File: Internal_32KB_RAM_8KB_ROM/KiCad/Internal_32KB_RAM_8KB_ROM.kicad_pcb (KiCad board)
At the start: 2 copper layers, 82.9 x 61 mm, 14 parts, among them J1 UD4, J2 UE4, J3 RAM Decoder, J4 BLK Decoder, J5 Disable/Enable Switch, U1 ATF16V8, U2 74HCT138, U3 62256, U4 2864

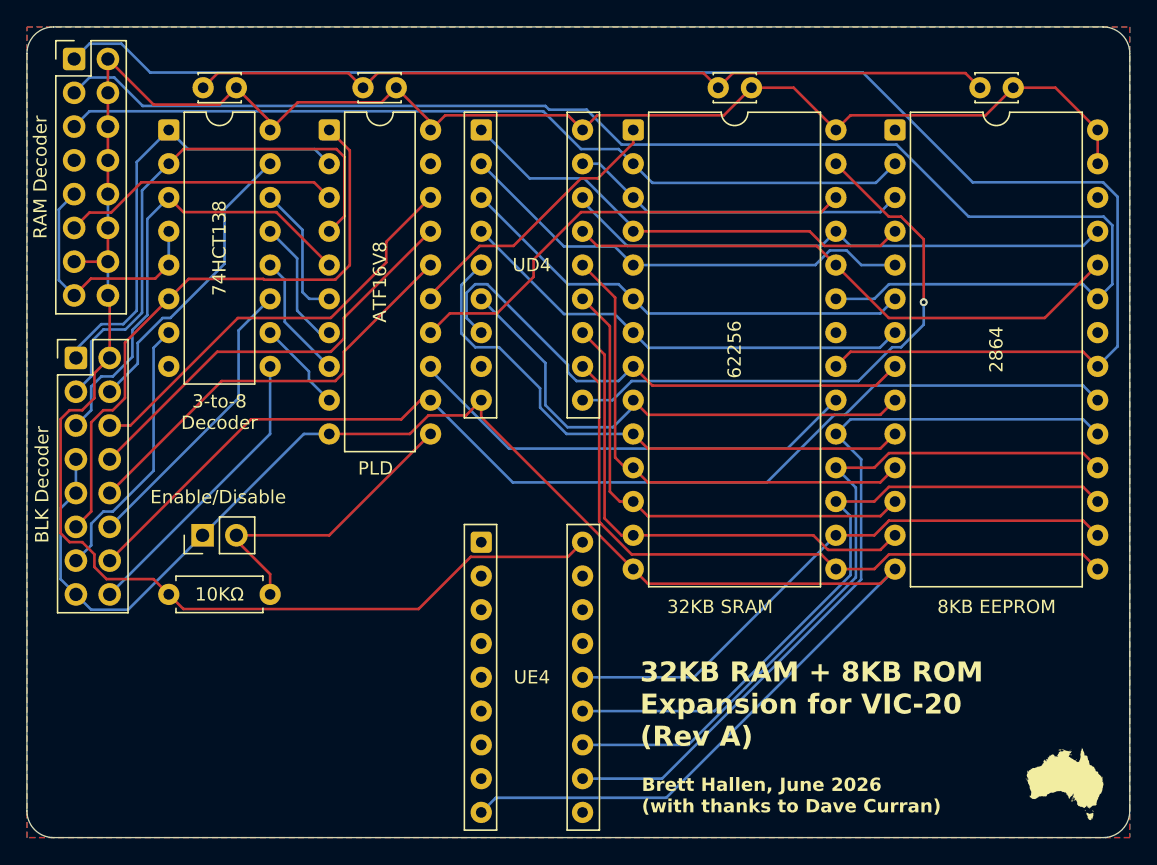
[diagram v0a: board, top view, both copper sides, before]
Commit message: Finalised 40KB design for testing
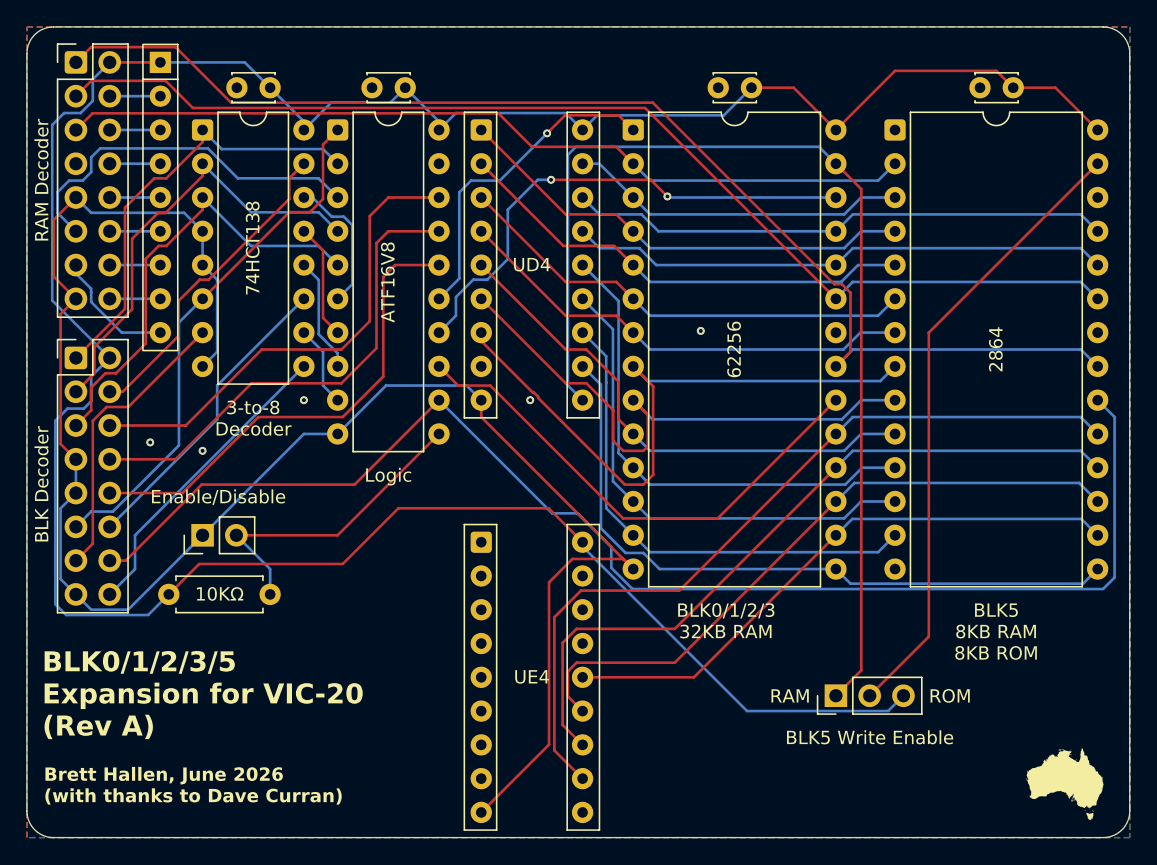
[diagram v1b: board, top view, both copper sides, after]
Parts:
- added J6: BLK5 Write Enable, Connector_PinHeader_2.54mm:PinHeader_1x03_P2.54mm_Vertical, F.Cu at (126.8, 83.2)
- added RN1: 10KΩ, Resistor_THT:R_Array_SIP9, F.Cu at (76.0, 35.6)
- moved C2 2.54 mm to (84.3, 37.5)
- moved U2 2.54 mm to (79.2, 40.6)
- moved C1 0.67 mm to (94.4, 37.5)
- moved U1 0.64 mm to (89.3, 40.6)
- moved J3 0.29 mm to (69.7, 35.6)
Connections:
- J3 pad 10: +5V -> Net-(J3-Pin_10)
- J3 pad 11: +5V -> Net-(J3-Pin_11)
- J3 pad 12: +5V -> Net-(J3-Pin_12)
- J3 pad 13: +5V -> Net-(J3-Pin_13)
- J3 pad 14: +5V -> Net-(J3-Pin_14)
- J3 pad 15: +5V -> Net-(J3-Pin_15)
- J3 pad 7: +5V -> Net-(J3-Pin_7)
- J3 pad 9: +5V -> Net-(J3-Pin_9)
- U4 pad 27: +5V -> ~{BLK5_W}
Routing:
- net GND: track 205.7 -> 137.4 mm, vias 0 -> 5
- net ~{BLK5_W}: track 0.00 -> 47.1 mm
- net VR/~{W}: track 43.4 -> 81.4 mm, vias 1 -> 0
- net +5V: track 174.3 -> 210.3 mm
- net VA11: track 109.7 -> 85.2 mm
- net VA10: track 117.7 -> 93.1 mm
- net ~{BLK5_OUT}: track 85.3 -> 101.6 mm
- net Net-(J3-Pin_7): track 0.00 -> 9.41 mm
- net CA14: track 41.0 -> 33.7 mm
- net VA13: track 21.1 -> 28.1 mm
- net VA2: track 40.9 -> 47.8 mm
- net SΦ2: track 46.1 -> 39.9 mm
- net VA1: track 39.0 -> 43.6 mm
- net ~{BLK2_OUT}: track 32.1 -> 36.5 mm
- net ~{BLK1_OUT}: track 32.1 -> 36.5 mm
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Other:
- board text added: "17-JUN-2026: Pending testing"
- board text added: "BLK0/1/2/3 32KB RAM"
- board text added: "BLK0/1/2/3/5 Expansion for VIC-20 (Rev A)"
- board text added: "BLK5 8KB RAM 8KB ROM"
- board text added: "Logic"
- board text added: "RAM"
- board text added: "ROM"
- board text removed: "12-JUN-2026: Pending testing"
- board text removed: "32KB RAM + 8KB ROM Expansion for VIC-20 (Rev A)"
- board text removed: "32KB SRAM"
- board text removed: "8KB EEPROM"
- board text removed: "PLD"
